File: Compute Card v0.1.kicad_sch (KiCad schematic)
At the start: 12 parts, among them J1 Bus_PCI_Express_x1, U1 PI7C9X440SLBFDE, U2 TPS62130A

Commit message: Almost Completed PCIe Interface
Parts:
- added C2, C3, C4, C5: 12pF, Capacitor_SMD:C_0603_1608Metric, symbol Device:C_Small
- added R10, R11, R12, R7, R8, R9: 4.7kΩ, Resistor_SMD:R_0805_2012Metric_Pad1.20x1.40mm_HandSolder, symbol Device:R
- added TP2, TP3, TP4, TP5, TP6, TP7, TP8: TestPoint, TestPoint:TestPoint_Pad_D1.0mm, symbol Connector:TestPoint
- added U3: CAT24C04C4ATR, WLCSP4_0P84X0P86_ONS:WLCSP4_0P84X0P86_ONS, symbol 2026-02-08_09-35-42:CAT24C04C4ATR
- added U4: RP2040, Package_DFN_QFN:QFN-56-1EP_7x7mm_P0.4mm_EP3.2x3.2mm_ThermalVias, symbol MCU_RaspberryPi:RP2040
- added Y1, Y2: WE-XTAL_CFPX-104, WE-XTAL_CFPX-104:WE-XTAL_CFPX-104, symbol WE-XTAL_CFPX-104:WE-XTAL_CFPX-104
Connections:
- net VSS is gone; now on net GND: U1.101 (VSS), U1.106 (VSS), U1.110 (VSS), U1.118 (VSS), U1.120 (VSS), U1.125 (VSS), U1.127 (VSS), U1.129 (VSS), U1.23 (VSS), U1.34 (VSS), U1.36 (VSS), U1.39 (VSS), U1.45 (VSS), U1.50 (VSS), U1.53 (VSS), U1.61 (VSS), U1.68 (VSS), U1.82 (VSS), U1.86 (VSS), U1.89 (VSS), U1.9 (VSS), U1.94 (VSS), U1.96 (VSS)
- net +3V3: now also R7.1, R8.1, R9.1, U3.A1 (VCC)
- net GND: now also C2.1, C3.2, C4.1, C5.2, R10.1, R11.1, R12.2, U3.A2 (VSS), U4.57 (GND), Y1.2, Y1.4, Y2.2, Y2.4
- net at U1.1 (TEST1): now also R10.2
- net at U1.102 (XI): now also C2.2, Y1.3
- net at U1.103 (XO): now also C3.1, Y1.1
- net at U1.114 (TEST5): now also R8.2
- net USB_D-: now reaches U1.123 (DM[1])
- net USB_D-: now also U4.46 (USB_DM)
- net USB_D+: now reaches U1.124 (DP[1])
- net USB_D+: now also U4.47 (USB_DP)
- net SMCLK: now reaches U1.21 (SMBCLK)
- net SMCLK: now also J1.B5 (SMCLK)
- net at U1.25 (TDO): now also TP6.1
- net at U1.26 (TCK): now also TP4.1
- net at U1.27 (TMS): now also TP5.1
- net at U1.28 (TDI): now also TP7.1
- net at U1.29 (TRST_L): now also R12.1, TP8.1
- net SMDAT: now reaches U1.64 (SMBDATA)
- net SMDAT: now also J1.B6 (SMDAT)
- net at U1.65 (TEST3): now also R7.2
- net at U1.66 (TEST6): now also R9.2
- net at U1.77 (TEST4): now also R11.2
- net at U1.98 (EEPD): now also TP2.1, U3.B2 (SDA)
- net at U1.99 (EECLK): now also TP3.1, U3.B1 (SCL)
- new net: U4.1 (IOVDD), U4.10 (IOVDD), U4.22 (IOVDD), U4.33 (IOVDD), U4.42 (IOVDD), U4.49 (IOVDD)
- new net: C5.1, U4.20 (XIN), Y2.1
- new net: C4.2, U4.21 (XOUT), Y2.3
- new net: U4.23 (DVDD), U4.50 (DVDD)
- no-connect marks 0 -> 15
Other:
- moved on the sheet: C1, J1, L1, R1, R2, R3, R4, R5, R6, TP1, U1, U2

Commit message: Added RP2ß40 as Main MCU
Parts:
- added R13, R14, R15, R16: 4.7kΩ, Resistor_SMD:R_0805_2012Metric_Pad1.20x1.40mm_HandSolder, symbol Device:R
- added R17: 5.9kΩ, Resistor_SMD:R_0603_1608Metric, symbol Device:R
- added R18: 137Ω, Resistor_SMD:R_1206_3216Metric, symbol Device:R
- added TP10, TP11, TP12, TP13, TP9: TestPoint, TestPoint:TestPoint_Pad_D1.0mm, symbol Connector:TestPoint
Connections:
- net +3V3: now also R13.2, R14.2, R15.2, R16.2
- net GND: now also R18.2
- net at U1.10 (POE[1]): now also TP9.1
- net at U1.119 (RREF[2]): now also TP11.1
- net at U1.126 (RREF[1]): now also R17.1
- net at U1.4 (OCI[1]): now also R13.1
- net at U1.5 (OCI[2]): now also R14.1
- net at U1.6 (OCI[3]): now also R15.1
- net at U1.7 (OCI[4]): now also R16.1
- net at U1.87 (RREF[4]): now also TP13.1
- net at U1.95 (RREF[3]): now also TP12.1
- new net: R17.2, R18.1, TP10.1
- no-connect marks 15 -> 18

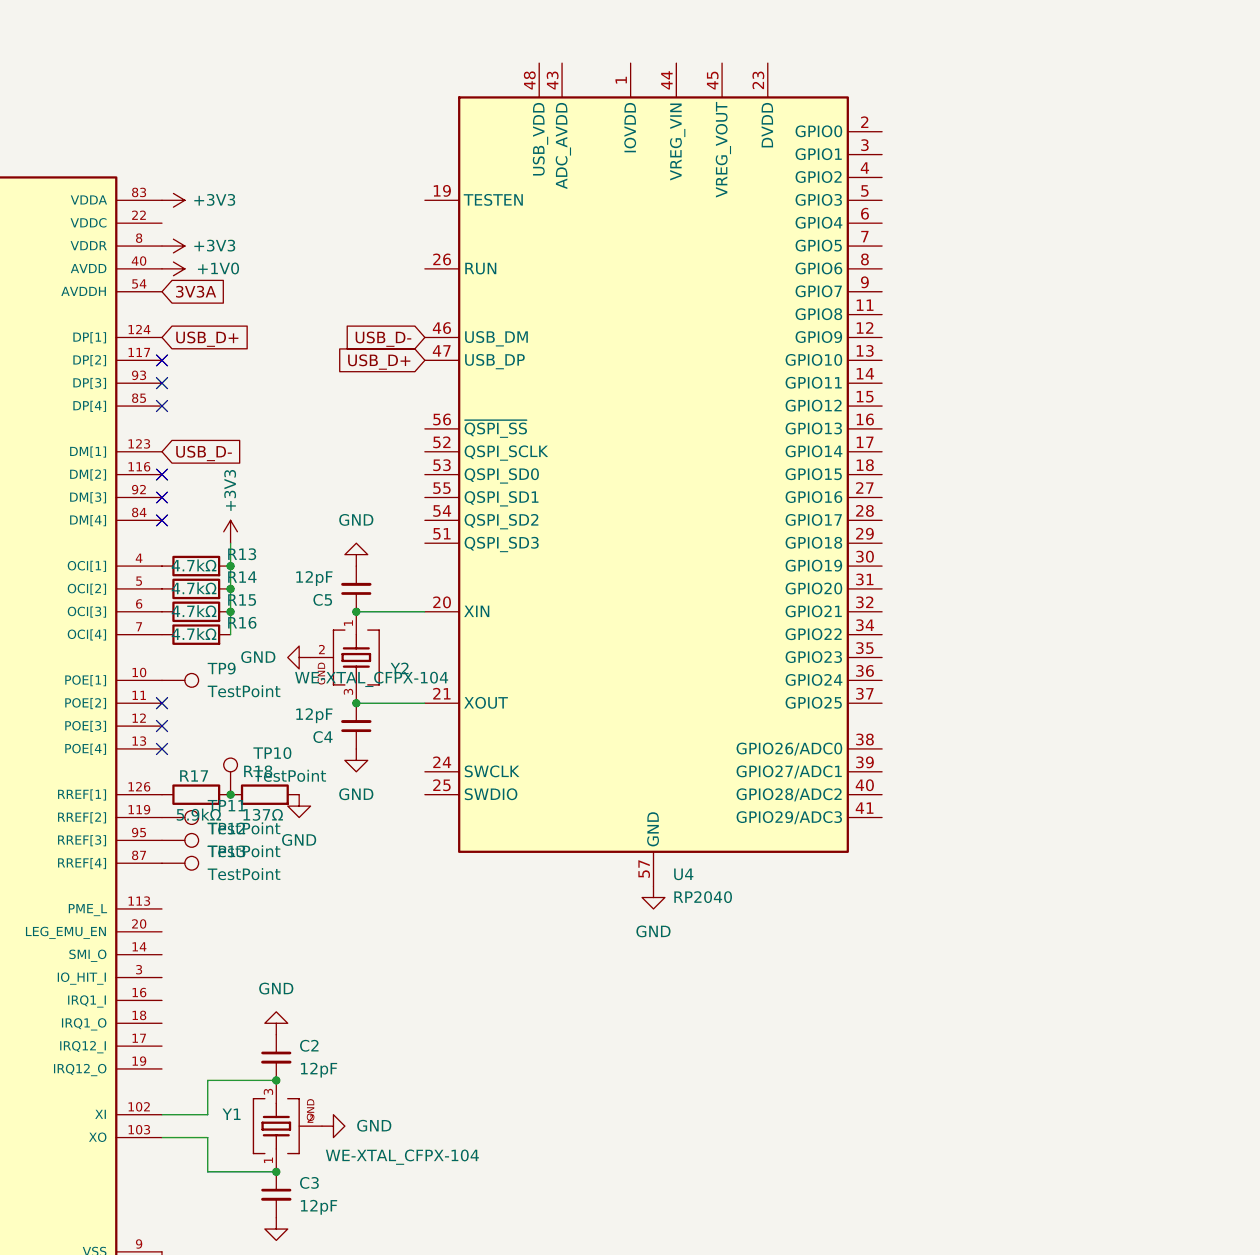
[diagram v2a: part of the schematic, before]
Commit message: Completed PCIe to USB Bridge
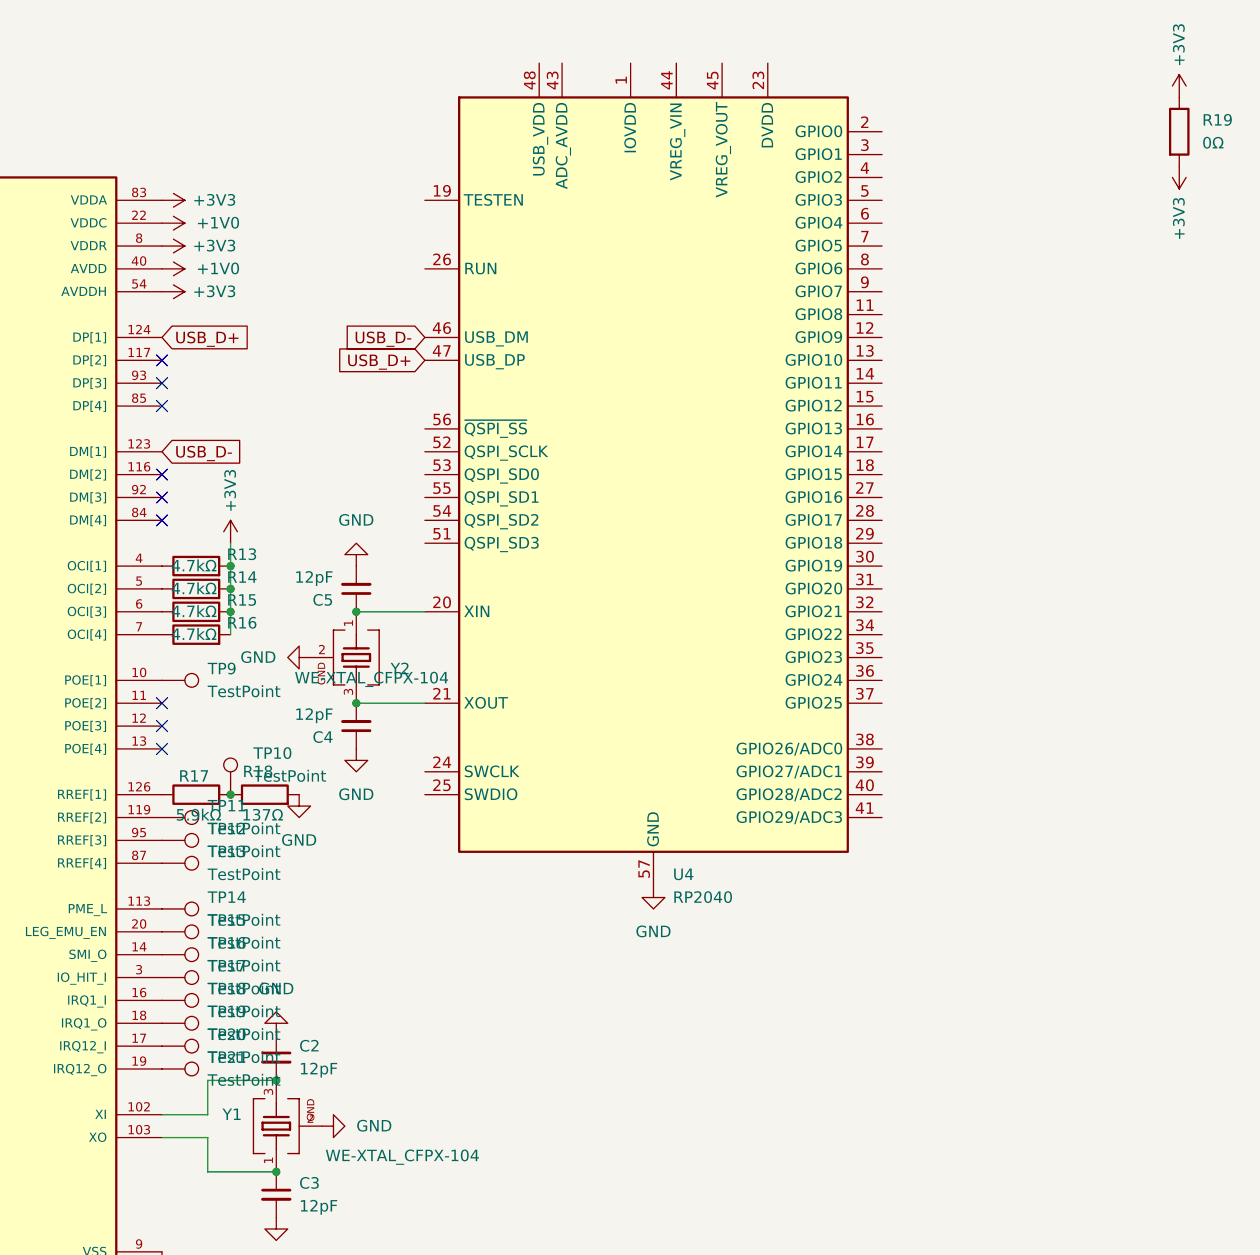
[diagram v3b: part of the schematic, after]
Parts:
- added R19: 0Ω, Resistor_SMD:R_0805_2012Metric, symbol Device:R
- added TP14, TP15, TP16, TP17, TP18, TP19, TP20, TP21: TestPoint, TestPoint:TestPoint_Pad_D1.0mm, symbol Connector:TestPoint
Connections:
- net 3V3A is gone; now on net +3V3: U1.54 (AVDDH)
- net VDDC is gone; now on net +1V0: U1.100 (VDDC), U1.109 (VDDC), U1.111 (VDDC), U1.22 (VDDC), U1.35 (VDDC), U1.81 (VDDC)
- net +3V3: now also R19.1, R19.2
- net at U1.113 (PME_L): now also TP14.1
- net at U1.14 (SMI_O): now also TP16.1
- net at U1.16 (IRQ1_I): now also TP18.1
- net at U1.17 (IRQ12_I): now also TP20.1
- net at U1.18 (IRQ1_O): now also TP19.1
- net at U1.19 (IRQ12_O): now also TP21.1
- net at U1.20 (LEG_EMU_EN): now also TP15.1
- net at U1.3 (IO_HIT_I): now also TP17.1
